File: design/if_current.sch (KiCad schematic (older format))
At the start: 8 parts

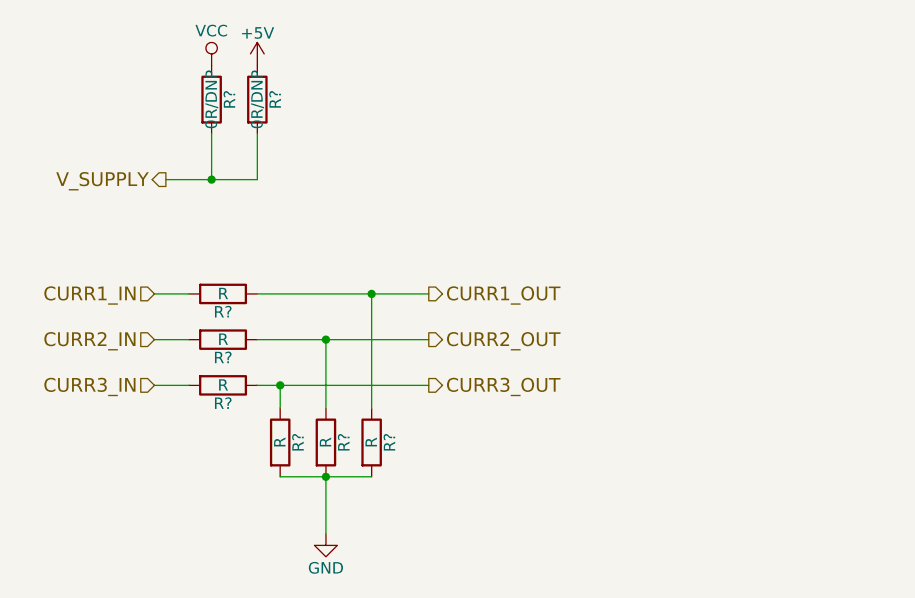
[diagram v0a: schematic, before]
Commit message: Removed 5V power level. Integrated isolated CAN bus driver.
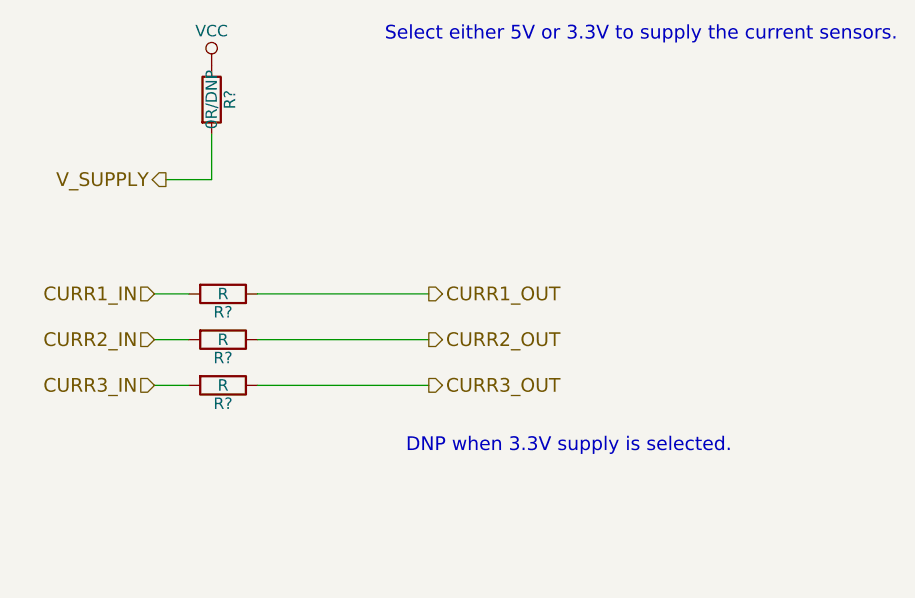
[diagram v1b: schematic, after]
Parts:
- removed R?: 0R/DNP, symbol R
- removed R? (x3): R, symbol R
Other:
- note added: "DNP when 3.3V supply is selected."
- note added: "Select either 5V or 3.3V to supply the current sensors."
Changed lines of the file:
@@
 CURR3_OUT
-$Comp
-L GND #PWR?
-U 1 1 56102E18
-P 7650 4900
-F 0 "#PWR?" H 7650 4650 50  0001 C CNN
-F 1 "GND" H 7650 4750 50  0000 C CNN
-F 2 "" H 7650 4900 60  0000 C CNN
-F 3 "" H 7650 4900 60  0000 C CNN
-	1    7650 4900
-	1    0    0    -1
-$EndComp
 $Comp
 L VCC #PWR?
@@
 F 3 "" H 7150 2850 60  0000 C CNN
 	1    7150 2850
-	1    0    0    -1
-$EndComp
-$Comp
-L +5V #PWR?
-U 1 1 56102E40
-P 7350 2850
-F 0 "#PWR?" H 7350 2700 50  0001 C CNN
-F 1 "+5V" H 7350 2990 50  0000 C CNN
-F 2 "" H 7350 2850 60  0000 C CNN
-F 3 "" H 7350 2850 60  0000 C CNN
-	1    7350 2850
 	1    0    0    -1
 $EndComp
@@
 	1    0    0    -1
 $EndComp
-$Comp
-L R R?
-U 1 1 56103335
-P 7350 3000
-F 0 "R?" V 7430 3000 50  0000 C CNN
-F 1 "0R/DNP" V 7350 3000 50  0000 C CNN
-F 2 "" V 7280 3000 30  0000 C CNN
-F 3 "" H 7350 3000 30  0000 C CNN
-	1    7350 3000
-	1    0    0    -1
-$EndComp
-Wire Wire Line
-	6950 3350 7350 3350
-Wire Wire Line
-	7150 3350 7150 3150
-Wire Wire Line
-	7350 3350 7350 3150
-Connection ~ 7150 3350
 $Comp
 L R R?
@@
 	0    1    1    0
 $EndComp
-$Comp
-L R R?
-U 1 1 56103695
-P 7450 4500
-F 0 "R?" V 7530 4500 50  0000 C CNN
-F 1 "R" V 7450 4500 50  0000 C CNN
-F 2 "" V 7380 4500 30  0000 C CNN
-F 3 "" H 7450 4500 30  0000 C CNN
-	1    7450 4500
-	1    0    0    -1
-$EndComp
-$Comp
-L R R?
-U 1 1 561036BA
-P 7650 4500
-F 0 "R?" V 7730 4500 50  0000 C CNN
-F 1 "R" V 7650 4500 50  0000 C CNN
-F 2 "" V 7580 4500 30  0000 C CNN
-F 3 "" H 7650 4500 30  0000 C CNN
-	1    7650 4500
-	1    0    0    -1
-$EndComp
-$Comp
-L R R?
-U 1 1 561036E7
-P 7850 4500
-F 0 "R?" V 7930 4500 50  0000 C CNN
-F 1 "R" V 7850 4500 50  0000 C CNN
-F 2 "" V 7780 4500 30  0000 C CNN
-F 3 "" H 7850 4500 30  0000 C CNN
-	1    7850 4500
-	1    0    0    -1
-$EndComp
 Wire Wire Line
 	6900 3850 7050 3850
@@
 Wire Wire Line
 	7350 4250 8100 4250
+Text Notes 10150 2750 2    60   ~ 0
+Select either 5V or 3.3V to supply the current sensors.
+Text Notes 8000 4550 0    60   ~ 0
+DNP when 3.3V supply is selected.
 Wire Wire Line
-	7450 4350 7450 4250
-Connection ~ 7450 4250
+	6950 3350 7150 3350
 Wire Wire Line
-	7650 4350 7650 4050
-Connection ~ 7650 4050
-Wire Wire Line
-	7850 4350 7850 3850
-Connection ~ 7850 3850
-Wire Wire Line
-	7450 4650 7850 4650
-Connection ~ 7650 4650
-Wire Wire Line
-	7650 4900 7650 4650
+	7150 3350 7150 3150
 $EndSCHEMATC

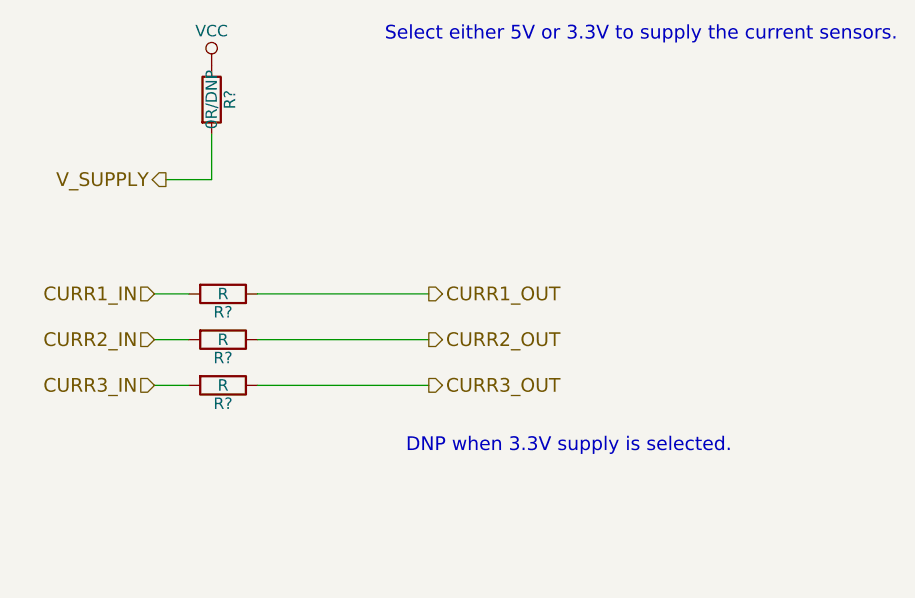
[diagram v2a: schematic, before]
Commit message: Assigned some footprints.
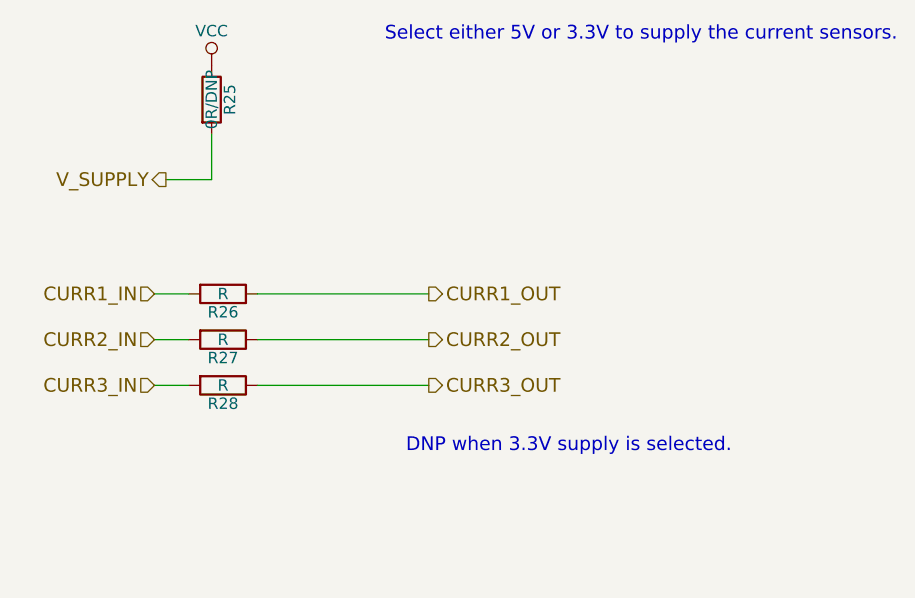
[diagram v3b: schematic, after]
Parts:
- gave numbers to parts that had none: 4
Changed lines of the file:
@@
 CURR3_OUT
 $Comp
-L VCC #PWR?
+L VCC #PWR046
 U 1 1 56102E2C
 P 7150 2850
-F 0 "#PWR?" H 7150 2700 50  0001 C CNN
+F 0 "#PWR046" H 7150 2700 50  0001 C CNN
 F 1 "VCC" H 7150 3000 50  0000 C CNN
 F 2 "" H 7150 2850 60  0000 C CNN
@@
 V_SUPPLY
 $Comp
-L R R?
+L R R25
 U 1 1 56103306
 P 7150 3000
-F 0 "R?" V 7230 3000 50  0000 C CNN
+F 0 "R25" V 7230 3000 50  0000 C CNN
 F 1 "0R/DNP" V 7150 3000 50  0000 C CNN
-F 2 "" V 7080 3000 30  0000 C CNN
+F 2 "" V 7080 3000 30  0001 C CNN
 F 3 "" H 7150 3000 30  0000 C CNN
 	1    7150 3000
@@
 $EndComp
 $Comp
-L R R?
+L R R26
 U 1 1 561035CE
 P 7200 3850
-F 0 "R?" V 7280 3850 50  0000 C CNN
+F 0 "R26" V 7280 3850 50  0000 C CNN
 F 1 "R" V 7200 3850 50  0000 C CNN
-F 2 "" V 7130 3850 30  0000 C CNN
+F 2 "" V 7130 3850 30  0001 C CNN
 F 3 "" H 7200 3850 30  0000 C CNN
 	1    7200 3850
@@
 $EndComp
 $Comp
-L R R?
+L R R27
 U 1 1 5610360F
 P 7200 4050
-F 0 "R?" V 7280 4050 50  0000 C CNN
+F 0 "R27" V 7280 4050 50  0000 C CNN
 F 1 "R" V 7200 4050 50  0000 C CNN
-F 2 "" V 7130 4050 30  0000 C CNN
+F 2 "" V 7130 4050 30  0001 C CNN
 F 3 "" H 7200 4050 30  0000 C CNN
 	1    7200 4050
@@
 $EndComp
 $Comp
-L R R?
+L R R28
 U 1 1 56103656
 P 7200 4250
-F 0 "R?" V 7280 4250 50  0000 C CNN
+F 0 "R28" V 7280 4250 50  0000 C CNN
 F 1 "R" V 7200 4250 50  0000 C CNN
-F 2 "" V 7130 4250 30  0000 C CNN
+F 2 "" V 7130 4250 30  0001 C CNN
 F 3 "" H 7200 4250 30  0000 C CNN
 	1    7200 4250

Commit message: Selected footprints
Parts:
- R25: footprint (none) -> Resistors_SMD:R_0603_HandSoldering
- R26, R27, R28: footprint (none) -> Resistors_SMD:R_0603
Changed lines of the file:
@@
 F 0 "R25" V 7230 3000 50  0000 C CNN
 F 1 "0R/DNP" V 7150 3000 50  0000 C CNN
-F 2 "" V 7080 3000 30  0001 C CNN
+F 2 "Resistors_SMD:R_0603_HandSoldering" V 7080 3000 30  0001 C CNN
 F 3 "" H 7150 3000 30  0000 C CNN
 	1    7150 3000
@@
 F 0 "R26" V 7280 3850 50  0000 C CNN
 F 1 "R" V 7200 3850 50  0000 C CNN
-F 2 "" V 7130 3850 30  0001 C CNN
+F 2 "Resistors_SMD:R_0603" V 7130 3850 30  0001 C CNN
 F 3 "" H 7200 3850 30  0000 C CNN
 	1    7200 3850
@@
 F 0 "R27" V 7280 4050 50  0000 C CNN
 F 1 "R" V 7200 4050 50  0000 C CNN
-F 2 "" V 7130 4050 30  0001 C CNN
+F 2 "Resistors_SMD:R_0603" V 7130 4050 30  0001 C CNN
 F 3 "" H 7200 4050 30  0000 C CNN
 	1    7200 4050
@@
 F 0 "R28" V 7280 4250 50  0000 C CNN
 F 1 "R" V 7200 4250 50  0000 C CNN
-F 2 "" V 7130 4250 30  0001 C CNN
+F 2 "Resistors_SMD:R_0603" V 7130 4250 30  0001 C CNN
 F 3 "" H 7200 4250 30  0000 C CNN
 	1    7200 4250
